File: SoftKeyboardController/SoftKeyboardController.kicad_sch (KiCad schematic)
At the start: 0 parts

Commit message: v1.0 Schematic
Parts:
- added C1: 470 μF, Capacitor_THT:C_Disc_D5.0mm_W2.5mm_P5.00mm, symbol Device:C_Small
- added C2: 0.1 μF, Capacitor_SMD:C_0805_2012Metric, symbol Device:C_Small
- added ESP1: ~, ME507F24:ESP32_NodeMCU_KeeYees, symbol ME507F24:ESP32_Node_KY
- added IC1: PCA9956BTWY, SOP50P640X110-39N, symbol SamacSys_Parts:PCA9956BTWY
- added J1: Barrel_Jack, Connector_BarrelJack:BarrelJack_SwitchcraftConxall_RAPC10U_Horizontal, symbol Connector:Barrel_Jack
- added J2: IMU Connection, Connector_Wire:SolderWire-0.15sqmm_1x05_P4mm_D0.5mm_OD1.5mm, symbol Connector_Generic:Conn_2Rows-05Pins
- added J3: Motor 1, TerminalBlock:TerminalBlock_Altech_AK300-2_P5.00mm, symbol Connector:Screw_Terminal_01x02
- added J4: Motor 2, TerminalBlock:TerminalBlock_Altech_AK300-2_P5.00mm, symbol Connector:Screw_Terminal_01x02
- added R1: 4.7 kΩ, Resistor_SMD:R_0805_2012Metric, symbol Device:R_Small_US
- added R3, R4: 330 mΩ, Resistor_SMD:R_0805_2012Metric, symbol Device:R_Small_US
- added R5: 10 kΩ, Resistor_SMD:R_0805_2012Metric, symbol Device:R_Small_US
- added U1: Motor Driver DRV8847PWR, Package_SO:TSSOP-16_4.4x5mm_P0.65mm, symbol Driver_Motor:DRV8847PWR
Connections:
- new net: C1.1, C2.2, J1.1, U1.12 (VM)
- new net: J4.1 (Pin_1), U1.7 (OUT3)
- new net: J4.2 (Pin_2), U1.5 (OUT4)
- new net: ESP1.23 (GPIO15), U1.11 (TRQ)
- new net: ESP1.24 (GPIO2), R1.2, U1.8 (~{FAULT})
- new net: ESP1.27 (GPIO16/RX2), U1.10 (IN4)
- new net: ESP1.28 (GPIO17/TX2), U1.9 (IN3)
- new net: ESP1.29 (GPIO5), U1.1 (~{SLEEP})
- new net: ESP1.30 (GPIO18/SCK), U1.15 (IN2)
- new net: ESP1.31 (GPIO19/CIPO), U1.16 (IN1)
- new net: ESP1.33 (GPIO21/SDA), IC1.37 (SDA), J2.2 (Pin_2)
- new net: ESP1.35 (GPIO1/TX0), IC1.35 (~{RESET}), J2.5 (Pin_5), R5.2
- new net: ESP1.36 (GPIO22/SCL), IC1.36 (SCL), J2.4 (Pin_4)
- new net: J3.1 (Pin_1), U1.2 (OUT1)
- new net: R3.2, U1.3 (ISEN12)
- new net: J3.2 (Pin_2), U1.4 (OUT2)
- new net: R4.2, U1.6 (ISEN34)
- new net +3V3: ESP1.1 (3V3), IC1.38 (VDD), J2.1 (Pin_1), R1.1, R5.1
- new net GND: C1.2, C2.1, ESP1.32 (GND), IC1.14 (VSS_1), IC1.18 (VSS_2), IC1.2 (AD0), IC1.21 (VSS_3), IC1.25 (VSS_4), IC1.3 (AD1), IC1.34 (VSS_5), IC1.39 (GND), IC1.4 (AD2), J1.2, J2.3 (Pin_3), R3.1, R4.1, U1.13 (GND), U1.14 (MODE)
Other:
- note added: "GND"
- note added: "SCL"
- note added: "SDA"
- note added: "Vin"
- note added: "nRESET"
- company: (none) -> ME 507
- title: (none) -> Soft Keyboard Platform Controller Schematic

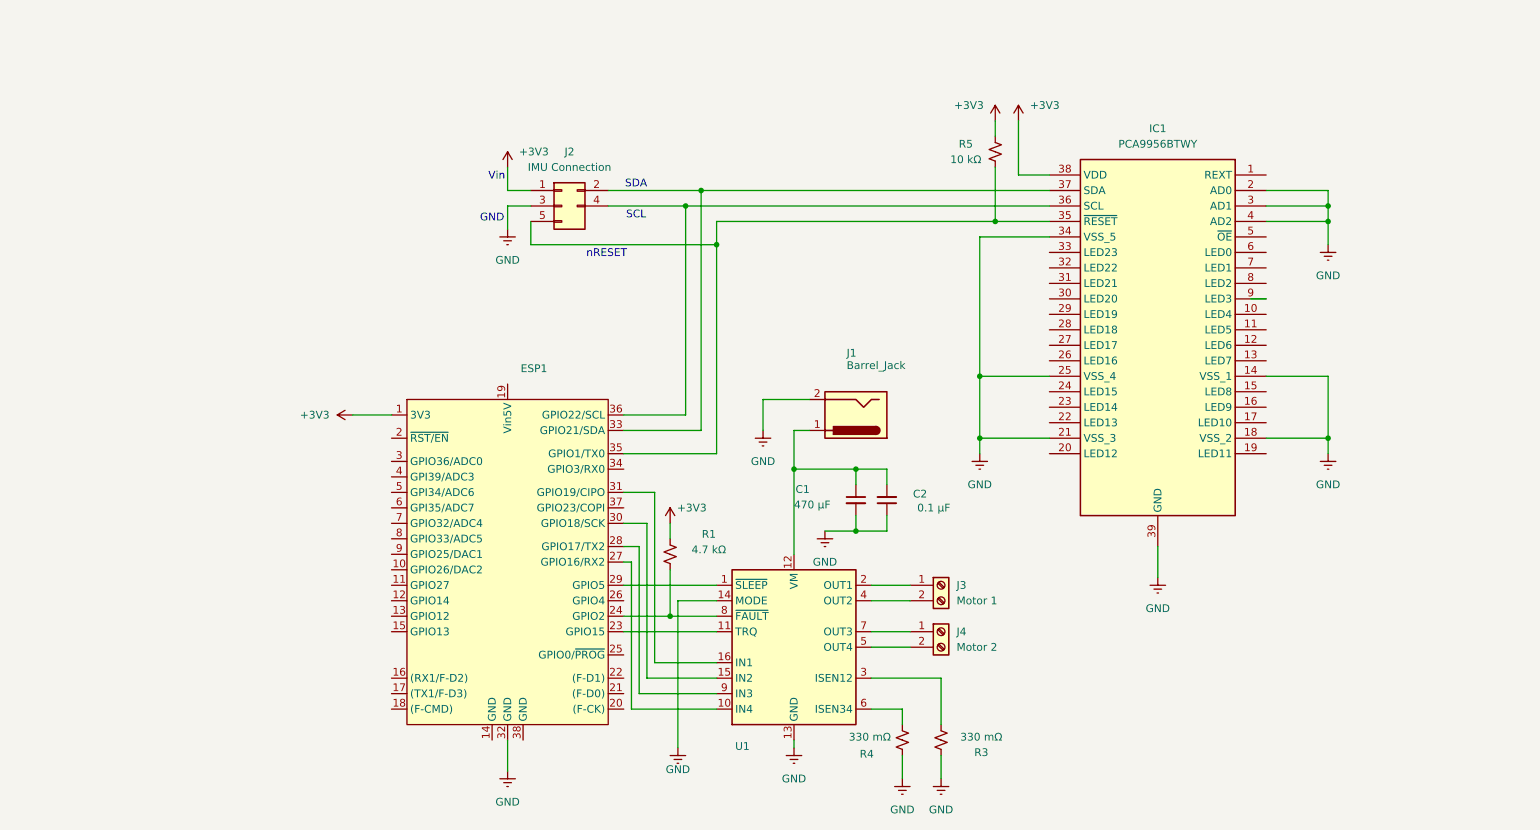
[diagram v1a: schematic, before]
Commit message: Update Schematic to v1.1 (redo of pull request)
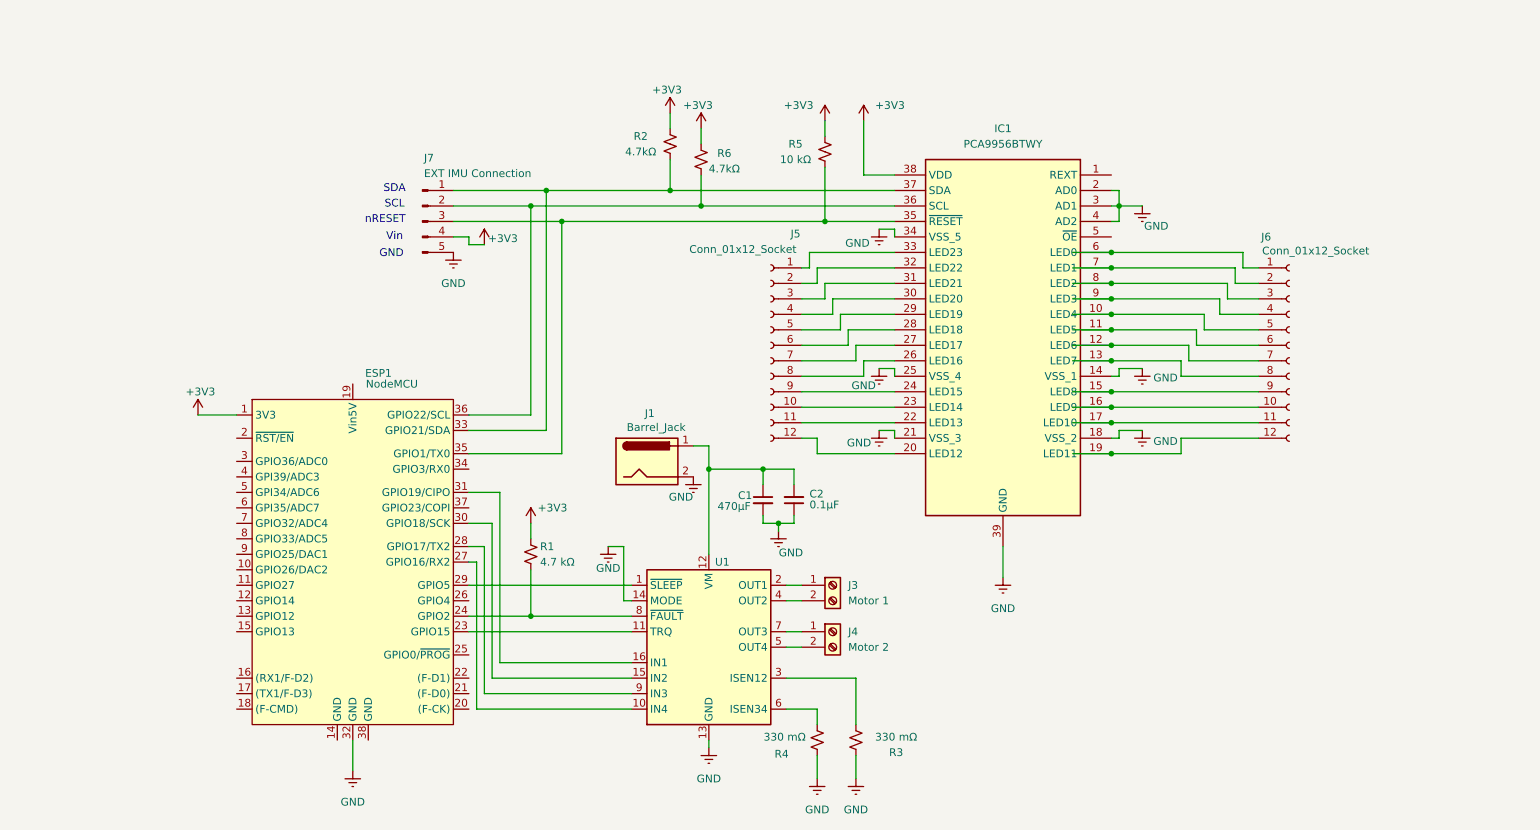
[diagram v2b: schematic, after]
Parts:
- removed J2: IMU Connection, Connector_Wire:SolderWire-0.15sqmm_1x05_P4mm_D0.5mm_OD1.5mm, symbol Connector_Generic:Conn_2Rows-05Pins
- added J5, J6: Conn_01x12_Socket, Connector_PinSocket_2.54mm:PinSocket_1x12_P2.54mm_Vertical, symbol Connector:Conn_01x12_Socket
- added J7: EXT IMU Connection, Connector_PinHeader_2.54mm:PinHeader_1x05_P2.54mm_Vertical, symbol Connector:Conn_01x05_Pin
- added R2, R6: 4.7kΩ, Resistor_SMD:R_0805_2012Metric, symbol Device:R_Small_US
- C1: value 470 μF -> 470μF
- C2: value 0.1 μF -> 0.1μF
- ESP1: value ~ -> NodeMCU
- J3, J4: footprint TerminalBlock:TerminalBlock_Altech_AK300-2_P5.00mm -> TerminalBlock_Phoenix:TerminalBlock_Phoenix_MKDS-1,5-2_1x02_P5.00mm_Horizontal
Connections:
- net +3V3: now also J7.4 (Pin_4), R2.1, R6.1
- net GND: now also J7.5 (Pin_5)
- net at ESP1.33 (GPIO21/SDA), IC1.37 (SDA): now also J7.1 (Pin_1), R2.2
- net at ESP1.35 (GPIO1/TX0), IC1.35 (~{RESET}), R5.2: now also J7.3 (Pin_3)
- net at ESP1.36 (GPIO22/SCL), IC1.36 (SCL): now also J7.2 (Pin_2), R6.2
- net at IC1.10 (LED4): now also J6.5 (Pin_5)
- net at IC1.11 (LED5): now also J6.6 (Pin_6)
- net at IC1.12 (LED6): now also J6.7 (Pin_7)
- net at IC1.13 (LED7): now also J6.8 (Pin_8)
- net at IC1.15 (LED8): now also J6.9 (Pin_9)
- net at IC1.16 (LED9): now also J6.10 (Pin_10)
- net at IC1.17 (LED10): now also J6.11 (Pin_11)
- net at IC1.19 (LED11): now also J6.12 (Pin_12)
- net at IC1.20 (LED12): now also J5.12 (Pin_12)
- net at IC1.22 (LED13): now also J5.11 (Pin_11)
- net at IC1.23 (LED14): now also J5.10 (Pin_10)
- net at IC1.24 (LED15): now also J5.9 (Pin_9)
- net at IC1.26 (LED16): now also J5.8 (Pin_8)
- net at IC1.27 (LED17): now also J5.7 (Pin_7)
- net at IC1.28 (LED18): now also J5.6 (Pin_6)
- net at IC1.29 (LED19): now also J5.5 (Pin_5)
- net at IC1.30 (LED20): now also J5.4 (Pin_4)
- net at IC1.31 (LED21): now also J5.3 (Pin_3)
- net at IC1.32 (LED22): now also J5.2 (Pin_2)
- net at IC1.33 (LED23): now also J5.1 (Pin_1)
- net at IC1.6 (LED0): now also J6.1 (Pin_1)
- net at IC1.7 (LED1): now also J6.2 (Pin_2)
- net at IC1.8 (LED2): now also J6.3 (Pin_3)
- net at IC1.9 (LED3): now also J6.4 (Pin_4)
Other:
- company: ME 507 -> CalPoly SLO ME 507 Fall 2025
- moved on the sheet: C1, C2, ESP1, IC1, J1, J3, J4, R1, R3, R4, R5, U1

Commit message: ADC chips
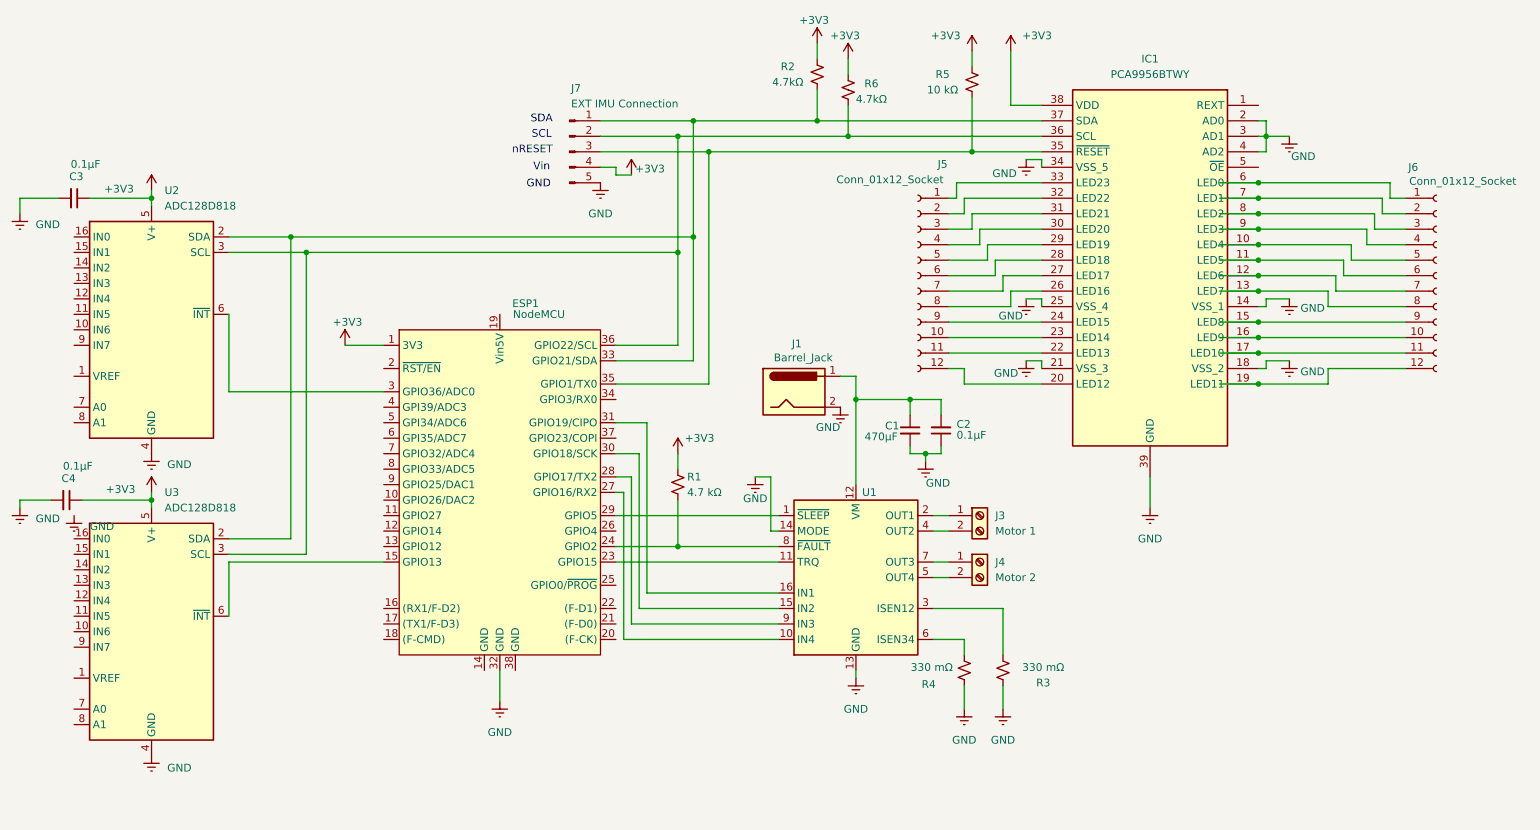
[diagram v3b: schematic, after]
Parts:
- added C3, C4: 0.1μF, Capacitor_SMD:C_0805_2012Metric, symbol Device:C_Small
- added U2, U3: ADC128D818, Package_SO:TSSOP-16_4.4x5mm_P0.65mm, symbol Analog_ADC:ADC128D818
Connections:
- net +3V3: now also C3.1, C4.1, U2.5 (V+), U3.5 (V+)
- net GND: now also C3.2, C4.2, U2.4 (GND), U3.4 (GND)
- net at ESP1.36 (GPIO22/SCL), IC1.36 (SCL), J7.2 (Pin_2)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: now also U2.3 (SCL), U3.3 (SCL)
- net at ESP1.15 (GPIO13): now also U3.6 (~{INT})
- net at ESP1.3 (GPIO36/ADC0): now also U2.6 (~{INT})
- net at ESP1.33 (GPIO21/SDA), IC1.37 (SDA), J7.1 (Pin_1)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: now also U2.2 (SDA), U3.2 (SDA)
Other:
- moved on the sheet: C1, C2, ESP1, IC1, J1, J3, J4, J5, J6, J7, R1, R2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
